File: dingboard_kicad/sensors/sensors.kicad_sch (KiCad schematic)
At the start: 45 parts, among them J1 Bus_PCI_Express_x1, J2 TYPE-C-31-M-04, J3 Conn_01x02, U1 BNO055, U2 RP2040, U3 TPS2121RUXR, U4 W25Q128JVP, U5 BME680, U6 LMR51430 1.1k FPWM, U7 MCP25625-x-SS, X1 ABM8-272-T3

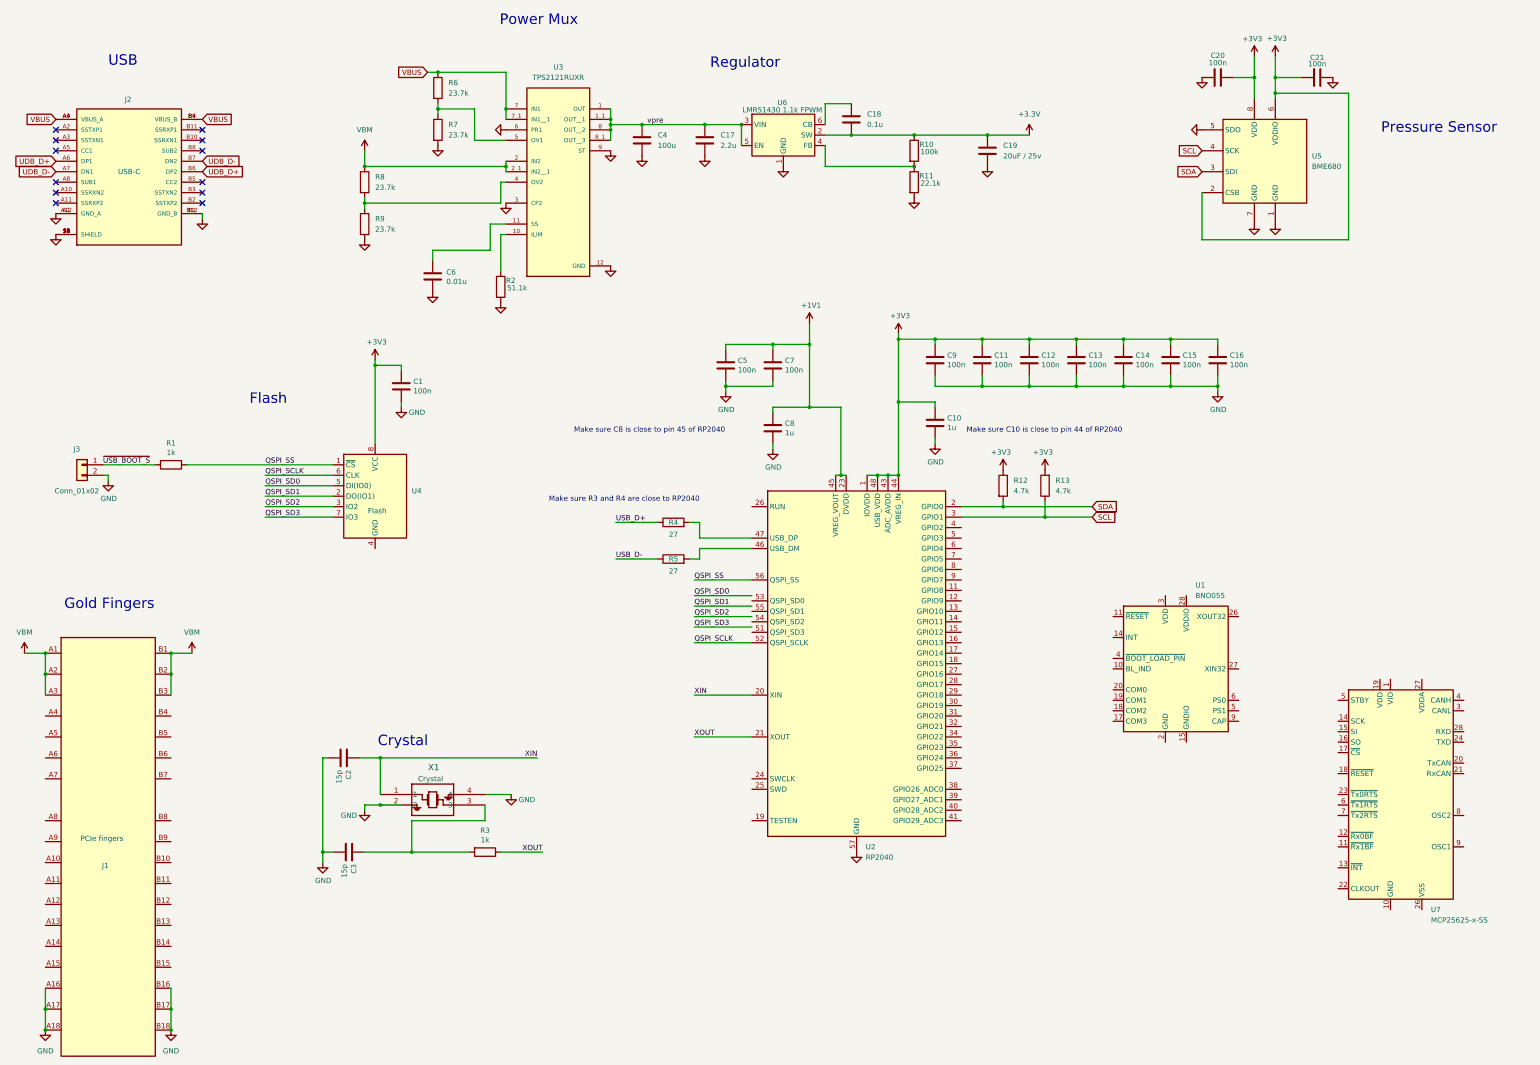
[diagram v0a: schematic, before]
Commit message: update BOM with new chip list
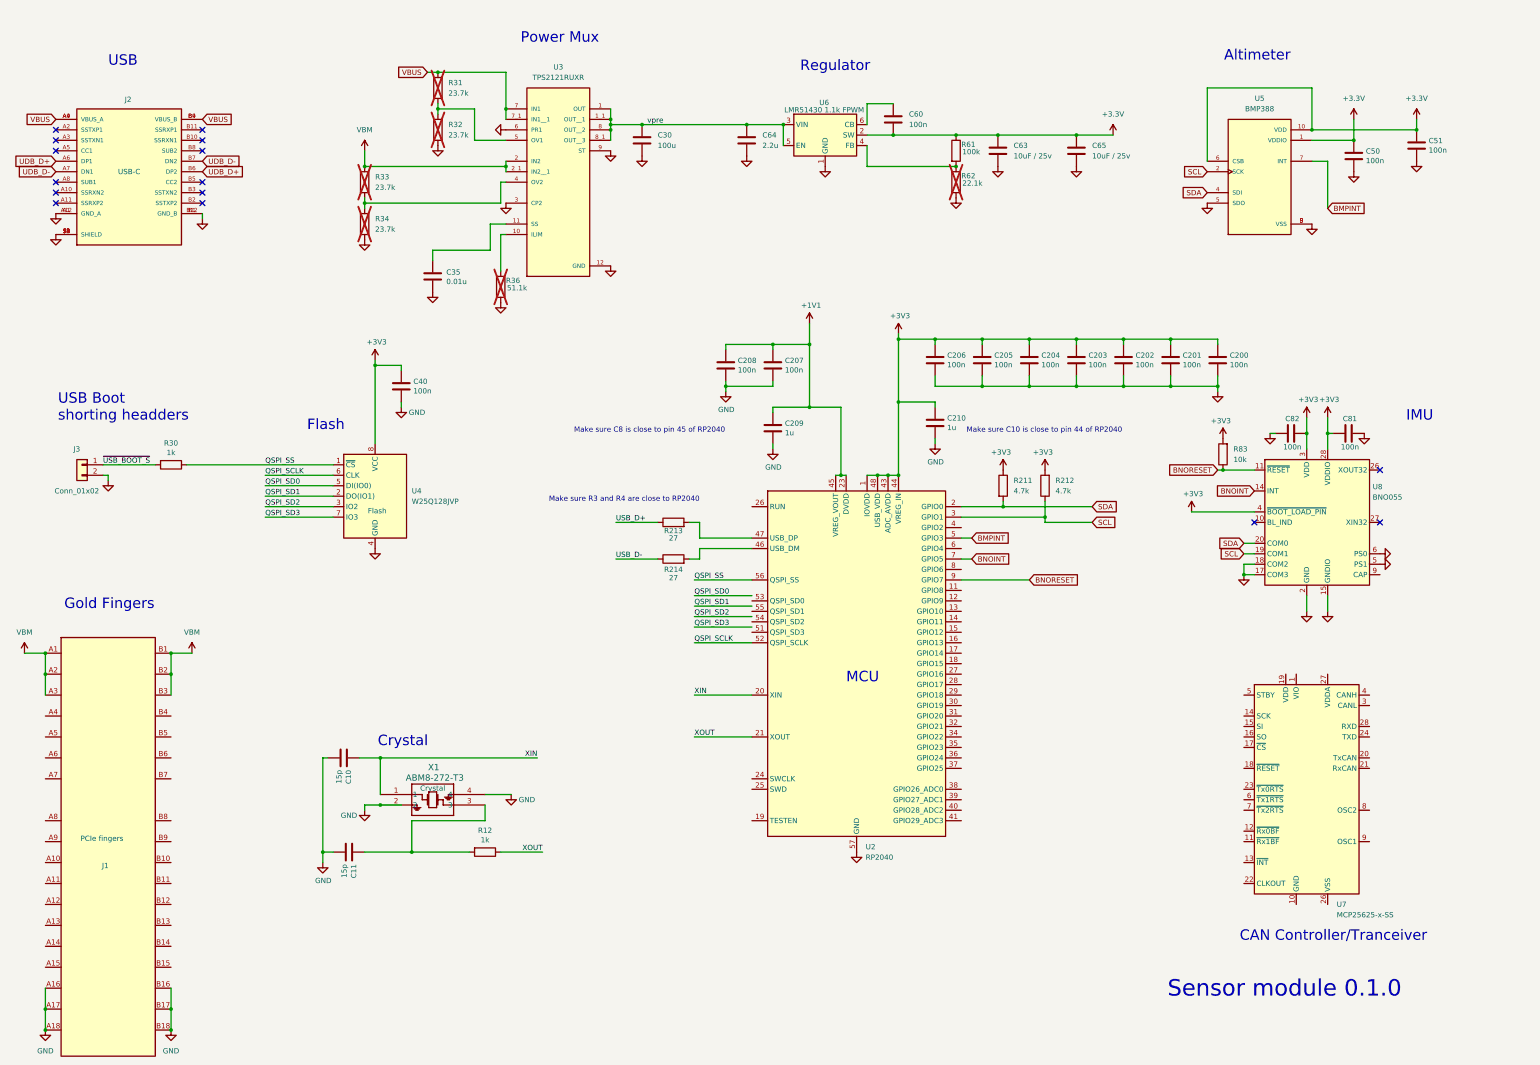
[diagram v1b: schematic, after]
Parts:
- removed C20, C21: 100n, Capacitor_SMD:C_0402_1005Metric, symbol Device:C
- removed U5: BME680, Package_LGA:Bosch_LGA-8_3x3mm_P0.8mm_ClockwisePinNumbering, symbol Sensor:BME680
- added C50, C51, C81, C82: 100n, Capacitor_SMD:C_0402_1005Metric, symbol Device:C
- added C65: 10uF / 25v, 0603, symbol Device:C
- added R83: 10k, Resistor_SMD:R_0402_1005Metric, symbol Device:R
- added U5: BMP388, BMP388:PQFN50P200X200X80-10N, symbol BMP388:BMP388
- C10: renamed from C2; LCSC Part # (none) -> C1548; basic? (none) -> yes; info (none) -> 15pF Cap; link (none) -> https://jlcpcb.com/partdetail/1900-0402CG150J500NT/C1548; price (none) -> C$0.0013
- C11: renamed from C3; LCSC Part # (none) -> C1548; basic? (none) -> yes; info (none) -> 15pF Cap; link (none) -> https://jlcpcb.com/partdetail/1900-0402CG150J500NT/C1548; price (none) -> C$0.0013
- C200: renamed from C16; LCSC Part # C1525 -> C307331; link (none) -> https://jlcpcb.com/partdetail/291005-CL05B104KB54PNC/C307331; price (none) -> C$0.0077
- C201: renamed from C15; LCSC Part # C1525 -> C307331; link (none) -> https://jlcpcb.com/partdetail/291005-CL05B104KB54PNC/C307331; price (none) -> C$0.0077
- C202: renamed from C14; LCSC Part # C1525 -> C307331; link (none) -> https://jlcpcb.com/partdetail/291005-CL05B104KB54PNC/C307331; price (none) -> C$0.0077
- C203: renamed from C13; LCSC Part # C1525 -> C307331; link (none) -> https://jlcpcb.com/partdetail/291005-CL05B104KB54PNC/C307331; price (none) -> C$0.0077
- C204: renamed from C12; LCSC Part # C1525 -> C307331; link (none) -> https://jlcpcb.com/partdetail/291005-CL05B104KB54PNC/C307331; price (none) -> C$0.0077
- C205: renamed from C11; LCSC Part # C1525 -> C307331; link (none) -> https://jlcpcb.com/partdetail/291005-CL05B104KB54PNC/C307331; price (none) -> C$0.0077
- C206: renamed from C9; LCSC Part # C1525 -> C307331; link (none) -> https://jlcpcb.com/partdetail/291005-CL05B104KB54PNC/C307331; price (none) -> C$0.0077
- C207: renamed from C7; LCSC Part # C1525 -> C307331; link (none) -> https://jlcpcb.com/partdetail/291005-CL05B104KB54PNC/C307331; price (none) -> C$0.0077
- C208: renamed from C5; LCSC Part # C1525 -> C307331; link (none) -> https://jlcpcb.com/partdetail/291005-CL05B104KB54PNC/C307331; price (none) -> C$0.0077
- C209: renamed from C8; basic? (none) -> yes; link (none) -> https://jlcpcb.com/partdetail/53938-CL05A105KA5NQNC/C52923; price (none) -> C$0.0041
- C210: renamed from C10; basic? (none) -> yes; link (none) -> https://jlcpcb.com/partdetail/53938-CL05A105KA5NQNC/C52923; price (none) -> C$0.0041
- C30: renamed from C4; footprint Capacitor_SMD:C_0402_1005Metric -> Capacitor_SMD:C_1206_3216Metric; LCSC Part # (none) -> C15008; basic? (none) -> yes; info (none) -> 100uF Cap; link (none) -> https://jlcpcb.com/partdetail/15681-CL31A107MQHNNNE/C15008; price (none) -> C$0.0830
- C35: renamed from C6; LCSC Part # (none) -> C15195; basic? (none) -> yes; info (none) -> 0.01uF Cap; link (none) -> https://jlcpcb.com/partdetail/15869-CL05B103KB5NNNC/C15195; price (none) -> C$0.0017
- C40: renamed from C1; LCSC Part # C1525 -> C307331; link (none) -> https://jlcpcb.com/partdetail/291005-CL05B104KB54PNC/C307331; price (none) -> C$0.0077
- C60: renamed from C18; value 0.1u -> 100n; LCSC Part # (none) -> C307331; basic? (none) -> yes; info (none) -> 100nF Cap; link (none) -> https://jlcpcb.com/partdetail/291005-CL05B104KB54PNC/C307331; price (none) -> C$0.0077
- C63: renamed from C19; value 20uF / 25v -> 10uF / 25v; footprint Capacitor_SMD:C_0402_1005Metric -> 0603; LCSC Part # (none) -> C96446; basic? (none) -> yes; info (none) -> 20uF / 25v cap; link (none) -> https://jlcpcb.com/partdetail/97651-CL10A106MA8NRNC/C96446; price (none) -> C$0.0226
- C64: renamed from C17; LCSC Part # (none) -> C12530; basic? (none) -> yes; info (none) -> 2.2uF Cap; link (none) -> https://jlcpcb.com/partdetail/13164-CL05A225MQ5NSNC/C12530; price (none) -> C$0.0031
- J3: basic? (none) -> n/a; link (none) -> n/a; price (none) -> n/a
- R12: renamed from R3; LCSC Part # (none) -> C11702; basic? (none) -> yes; info (none) -> 1k ohm; link (none) -> https://jlcpcb.com/partdetail/12256-0402WGF1001TCE/C11702; price (none) -> C$0.0007
- R211: renamed from R12; LCSC Part # (none) -> C25900; basic? (none) -> yes; info (none) -> 4.7k ohm; link (none) -> https://jlcpcb.com/partdetail/26643-0402WGF4701TCE/C25900; price (none) -> C$0.0007
- R212: renamed from R13; LCSC Part # (none) -> C25900; basic? (none) -> yes; info (none) -> 4.7k ohm; link (none) -> https://jlcpcb.com/partdetail/26643-0402WGF4701TCE/C25900; price (none) -> C$0.0007
- R213: renamed from R4; footprint Resistor_SMD:R_0402_1005Metric -> Resistor_SMD:R_0603_1608Metric; LCSC Part # (none) -> C25190; basic? (none) -> extended prefered; info (none) -> 27 ohm; link (none) -> https://jlcpcb.com/partdetail/25933-0603WAF270JT5E/C25190; price (none) -> C$0.0013
- R214: renamed from R5; footprint Resistor_SMD:R_0402_1005Metric -> Resistor_SMD:R_0603_1608Metric; LCSC Part # (none) -> C25190; basic? (none) -> extended prefered; info (none) -> 27 ohm; link (none) -> https://jlcpcb.com/partdetail/25933-0603WAF270JT5E/C25190; price (none) -> C$0.0013
- R30: renamed from R1; LCSC Part # (none) -> C11702; basic? (none) -> yes; info (none) -> 1k ohm; link (none) -> https://jlcpcb.com/partdetail/12256-0402WGF1001TCE/C11702; price (none) -> C$0.0007
- R31: renamed from R6; footprint Resistor_SMD:R_0402_1005Metric -> 0603; LCSC Part # (none) -> C22912; basic? (none) -> no; info (none) -> 23.7k ohm; link (none) -> https://jlcpcb.com/partdetail/23639-0603WAF2372T5E/C22912; price (none) -> C$0.0013; now not fitted
- R32: renamed from R7; footprint Resistor_SMD:R_0402_1005Metric -> 0603; LCSC Part # (none) -> C22912; basic? (none) -> no; info (none) -> 23.7k ohm; link (none) -> https://jlcpcb.com/partdetail/23639-0603WAF2372T5E/C22912; price (none) -> C$0.0013; now not fitted
- R33: renamed from R8; footprint Resistor_SMD:R_0402_1005Metric -> 0603; LCSC Part # (none) -> C22912; basic? (none) -> no; info (none) -> 23.7k ohm; link (none) -> https://jlcpcb.com/partdetail/23639-0603WAF2372T5E/C22912; price (none) -> C$0.0013; now not fitted
- R34: renamed from R9; footprint Resistor_SMD:R_0402_1005Metric -> 0603; LCSC Part # (none) -> C22912; basic? (none) -> no; info (none) -> 23.7k ohm; link (none) -> https://jlcpcb.com/partdetail/23639-0603WAF2372T5E/C22912; price (none) -> C$0.0013; now not fitted
- R36: renamed from R2; footprint Resistor_SMD:R_0402_1005Metric -> 0603; LCSC Part # (none) -> C23072; basic? (none) -> no; info (none) -> 51.1k ohm; link (none) -> https://jlcpcb.com/partdetail/23799-0603WAF5112T5E/C23072; price (none) -> C$0.0013; now not fitted
- R61: renamed from R10; LCSC Part # (none) -> C25741; basic? (none) -> yes; info (none) -> 100k ohm; link (none) -> https://jlcpcb.com/partdetail/26484-0402WGF1003TCE/C25741; price (none) -> C$0.0007
- R62: renamed from R11; footprint Resistor_SMD:R_0402_1005Metric -> 0603; LCSC Part # (none) -> C25961; basic? (none) -> no; info (none) -> 22.1k ohm; link (none) -> https://jlcpcb.com/partdetail/26704-0603WAF2212T5E/C25961; price (none) -> C$0.0013; now not fitted
- U3: link (none) -> https://jlcpcb.com/partdetail/TexasInstruments-TPS2121RUXR/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; price (none) -> C$1.3394
- U7: link (none) -> https://jlcpcb.com/partdetail/MicrochipTech-MCP25625_ESS/C1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; price (none) -> C$6.0709
- renumbered U1 to U8
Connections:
- net +3.3V: now also C50.1, C51.1, C65.1, U5.1 (VDDIO), U5.10 (VDD), U5.6 (CSB)
- net +3V3: now also U8.28 (VDDIO), U8.3 (VDD), U8.4 (~{BOOT_LOAD_PIN}), C81.1, C82.2, R83.2
- net GND: now also U4.4 (GND), U8.15 (GNDIO), U8.16 (GNDIO), U8.17 (COM3), U8.18 (COM2), U8.2 (GND), U8.25 (GNDIO), U8.5 (PS1), U8.6 (PS0), C50.2, C51.2, C65.2, C81.2, C82.1, U5.3 (VSS), U5.5 (SDO), U5.8 (VSS), U5.9 (VSS)
- net SCL: now also U8.19 (COM1), U5.2 (SCK)
- net SDA: now also U8.20 (COM0), U5.4 (SDI)
- net BNORESET: now reaches U8.11 (~{RESET})
- net BNORESET: now also U2.9 (GPIO7), R83.1
- net BNOINT: now reaches U8.14 (INT)
- net BNOINT: now also U2.7 (GPIO5)
- net BMPINT: now reaches U2.5 (GPIO3)
- net BMPINT: now also U5.7 (INT)
- no-connect marks 12 -> 15
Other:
- note added: "Altimeter"
- note added: "CAN Controller/Tranceiver"
- note added: "IMU"
- note added: "MCU"
- note added: "Sensor module 0.1.0"
- note added: "USB Boot shorting headders"
- note removed: "Pressure Sensor"
- moved on the sheet: C60, C63, C64, R61, U6, U7, U8
